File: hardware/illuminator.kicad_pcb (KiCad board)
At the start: 4 copper layers, 85 x 100 mm, 63 parts, among them J101 HRO_TYPE_C_31_M_12, J102 PROG, J103 LCLV, Q201 DMP3028, Q202 MMBT3904, SW101 RESET, SW102 DFU, U101 SRV05-4, U102 STM32G431CBUx, U103 WAS3157B-6/TR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

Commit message: heatsinking
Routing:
- net GND: vias 46 -> 48
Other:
- board text added: "mateijordache.info"
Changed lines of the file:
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@@
 		(fp_arc
 			(start 10.656836 20.999983)
-			(mid 9.891462 20.847753)
+			(mid 9.891468 20.847747)
 			(end 9.242623 20.414196)
 			(stroke
@@
 		(fp_arc
 			(start 30.160875 53.5)
-			(mid 28.989302 56.328429)
+			(mid 28.989302 56.328425)
 			(end 26.160875 57.5)
 			(stroke
@@
 		(tags "tag connect programming header pogo pins")
 		(property "Reference" "J102"
-			(at 0 -2.7 270)
+			(at 0 -2.7 -90)
 			(layer "B.SilkS")
 			(hide yes)
@@
 		)
 		(property "Value" "PROG"
-			(at 0 2.300001 270)
+			(at 0 2.300001 -90)
 			(layer "B.Fab")
 			(effects
@@
 		)
 		(fp_text user "KEEPOUT"
-			(at 0 0 270)
+			(at 0 0 -90)
 			(layer "Cmts.User")
 			(effects
@@
 		)
 		(fp_text user "${REFERENCE}"
-			(at 0 0 270)
+			(at 0 0 -90)
 			(layer "B.Fab")
 			(effects
@@
 		(net 7)
 	)
+	(gr_arc
+		(start 136.5985 121.498499)
+		(mid 150.421081 57.916367)
+		(end 164.91972 121.347753)
+		(stroke
+			(width 12)
+			(type default)
+		)
+		(layer "B.Mask")
+	)
+	(gr_text "mateijordache.info"
+		(at 161.4235 115.0735 0)
+		(layer "B.Mask")
+		(effects
+			(font
+				(size 1.5 1.5)
+				(thickness 0.3)
+				(bold yes)
+			)
+			(justify left bottom mirror)
+		)
+	)
 	(segment
 		(start 150.7485 145.5235)
@@
 	)
 	(segment
-		(start 146.0485 146.4985)
-		(end 150.7485 146.4985)
-		(width 0.25)
-		(layer "B.Cu")
-		(net 1)
-	)
-	(segment
 		(start 137.6485 137.8985)
 		(end 144.5885 137.8985)
@@
 	)
 	(segment
-		(start 145.3235 145.7735)
-		(end 146.0485 146.4985)
-		(width 0.25)
-		(layer "B.Cu")
-		(net 1)
-	)
-	(segment
 		(start 151.0235 145.5235)
 		(end 151.0485 145.4985)
@@
 	)
 	(segment
-		(start 136.1585 134.1585)
-		(end 135.4985 134.8185)
+		(start 145.2985 138.6085)
+		(end 145.3235 138.6335)
+		(width 0.25)
+		(layer "B.Cu")
+		(net 1)
+	)
+	(segment
+		(start 146.7985 146.4985)
+		(end 150.7485 146.4985)
 		(width 0.25)
 		(layer "B.Cu")
@@
 	(segment
 		(start 145.3235 138.6335)
-		(end 145.3235 145.7735)
+		(end 145.3235 145.0235)
 		(width 0.25)
 		(layer "B.Cu")
@@
 	)
 	(segment
-		(start 145.2985 138.6085)
-		(end 145.3235 138.6335)
+		(start 136.1585 134.1585)
+		(end 135.4985 134.8185)
+		(width 0.25)
+		(layer "B.Cu")
+		(net 1)
+	)
+	(segment
+		(start 145.3235 145.0235)
+		(end 146.7985 146.4985)
 		(width 0.25)
 		(layer "B.Cu")
@@
 	)
 	(via
+		(at 155.4985 137.1735)
+		(size 0.8)
+		(drill 0.4)
+		(layers "F.Cu" "B.Cu")
+		(free yes)
+		(net 2)
+	)
+	(via
 		(at 149.2985 141.0485)
 		(size 0.8)
@@
 	)
 	(via
+		(at 155.4985 138.6985)
+		(size 0.8)
+		(drill 0.4)
+		(layers "F.Cu" "B.Cu")
+		(free yes)
+		(net 2)
+	)
+	(via
 		(at 177.5735 108.6235)
 		(size 0.8)
@@
 	)
 	(segment
-		(start 159.7985 131.3985)
-		(end 159.7985 136.886)
+		(start 154.7485 117.8635)
+		(end 154.7485 118.9235)
 		(width 0.25)
 		(layer "B.Cu")
@@
 	)
 	(segment
-		(start 154.7485 119.0485)
-		(end 157.2235 121.5235)
+		(start 154.7485 118.9235)
+		(end 156.8485 121.0235)
 		(width 0.25)
 		(layer "B.Cu")
@@
 	)
 	(segment
-		(start 154.7485 117.8635)
-		(end 154.7485 119.0485)
+		(start 156.8485 121.0235)
+		(end 156.8485 128.711)
 		(width 0.25)
 		(layer "B.Cu")
@@
 	)
 	(segment
-		(start 157.2235 128.8235)
-		(end 159.7985 131.3985)
+		(start 159.5485 131.411)
+		(end 159.5485 136.636)
 		(width 0.25)
 		(layer "B.Cu")
@@
 	)
 	(segment
-		(start 159.7985 136.886)
+		(start 159.5485 136.636)
 		(end 161.4985 138.586)
 		(width 0.25)
@@
 	)
 	(segment
-		(start 157.2235 121.5235)
-		(end 157.2235 128.8235)
+		(start 156.8485 128.711)
+		(end 159.5485 131.411)
 		(width 0.25)
 		(layer "B.Cu")
@@
 	)
 	(segment
+		(start 144.7985 129.3485)
+		(end 139.9885 134.1585)
+		(width 0.1)
+		(layer "B.Cu")
+		(net 32)
+	)
+	(segment
 		(start 153.0235 129.4235)
 		(end 152.9485 129.3485)
@@
 	)
 	(segment
-		(start 152.9485 129.3485)
-		(end 142.2385 129.3485)
+		(start 139.9885 134.1585)
+		(end 137.4285 134.1585)
 		(width 0.1)
 		(layer "B.Cu")
@@
 	)
 	(segment
-		(start 142.2385 129.3485)
-		(end 137.4285 134.1585)
+		(start 152.9485 129.3485)
+		(end 144.7985 129.3485)
 		(width 0.1)
 		(layer "B.Cu")
@@
 	)
 	(segment
-		(start 152.4485 128.8485)
-		(end 141.4685 128.8485)
+		(start 144.5235 128.8485)
+		(end 140.4835 132.8885)
 		(width 0.1)
 		(layer "B.Cu")
@@
 	)
 	(segment
-		(start 141.4685 128.8485)
+		(start 140.4835 132.8885)
 		(end 137.4285 132.8885)
 		(width 0.1)
@@
 	)
 	(segment
+		(start 152.4485 128.8485)
+		(end 144.5235 128.8485)
+		(width 0.1)
+		(layer "B.Cu")
+		(net 33)
+	)
+	(segment
 		(start 145.3485 135.6985)
 		(end 145.0235 136.0235)
@@
 	)
 	(segment
-		(start 141.3235 128.1235)
-		(end 137.8285 131.6185)
+		(start 151.9485 128.1235)
+		(end 144.4235 128.1235)
 		(width 0.1)
 		(layer "B.Cu")
@@
 	)
 	(segment
-		(start 151.9485 128.1235)
-		(end 141.3235 128.1235)
+		(start 140.9285 131.6185)
+		(end 137.4285 131.6185)
 		(width 0.1)
 		(layer "B.Cu")
@@
 	)
 	(segment
-		(start 137.8285 131.6185)
-		(end 137.4285 131.6185)
+		(start 144.4235 128.1235)
+		(end 140.9285 131.6185)
 		(width 0.1)
 		(layer "B.Cu")
@@
 	)
 	(segment
-		(start 166.8735 144.1985)
-		(end 166.8735 141.8485)
+		(start 168.7235 139.9985)
+		(end 172.2765 139.9985)
 		(width 0.1)
 		(layer "B.Cu")
@@
 	)
 	(segment
-		(start 146.0235 137.8735)
-		(end 146.5235 138.3735)
-		(width 0.1)
-		(layer "B.Cu")
-		(net 42)
-	)
-	(segment
-		(start 166.8735 141.8485)
-		(end 168.7235 139.9985)
+		(start 150.4735 144.5985)
+		(end 166.4735 144.5985)
 		(width 0.1)
 		(layer "B.Cu")
@@
 	)
 	(segment
-		(start 146.9485 145.7235)
-		(end 148.817954 145.7235)
+		(start 146.0235 137.8735)
+		(end 146.0235 144.8235)
 		(width 0.1)
 		(layer "B.Cu")
@@
 	)
 	(segment
-		(start 168.7235 139.9985)
-		(end 172.2765 139.9985)
+		(start 166.8735 141.8485)
+		(end 168.7235 139.9985)
 		(width 0.1)
 		(layer "B.Cu")
@@
 	)
 	(segment
-		(start 148.817954 145.7235)
-		(end 149.942954 144.5985)
+		(start 166.4735 144.5985)
+		(end 166.8735 144.1985)
 		(width 0.1)
 		(layer "B.Cu")
@@
 	)
 	(segment
-		(start 146.5235 145.2985)
-		(end 146.9485 145.7235)
+		(start 146.0235 144.8235)
+		(end 147.0985 145.8985)
 		(width 0.1)
 		(layer "B.Cu")
@@
 	)
 	(segment
-		(start 146.5235 138.3735)
-		(end 146.5235 145.2985)
+		(start 147.0985 145.8985)
+		(end 149.1735 145.8985)
 		(width 0.1)
 		(layer "B.Cu")
@@
 	)
 	(segment
-		(start 149.942954 144.5985)
-		(end 166.4735 144.5985)
+		(start 149.1735 145.8985)
+		(end 150.4735 144.5985)
 		(width 0.1)
 		(layer "B.Cu")
@@
 	)
 	(segment
-		(start 166.4735 144.5985)
-		(end 166.8735 144.1985)
+		(start 166.8735 144.1985)
+		(end 166.8735 141.8485)
 		(width 0.1)
 		(layer "B.Cu")

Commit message: fix bom
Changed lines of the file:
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@@
 			(viasonmask no)
 			(mode 1)
-			(useauxorigin no)
+			(useauxorigin yes)
 			(hpglpennumber 1)
 			(hpglpenspeed 20)
@@
 			(outputformat 1)
 			(mirror no)
-			(drillshape 1)
+			(drillshape 0)
 			(scaleselection 1)
-			(outputdirectory "")
+			(outputdirectory "/Users/mateijordache/Desktop/gerbs/")
 		)
 	)
@@
 		(fp_arc
 			(start 10.656836 20.999983)
-			(mid 9.891468 20.847747)
+			(mid 9.891462 20.847753)
 			(end 9.242623 20.414196)
 			(stroke
@@
 		(fp_arc
 			(start 30.160875 53.5)
-			(mid 28.989302 56.328425)
+			(mid 28.989302 56.328429)
 			(end 26.160875 57.5)
 			(stroke

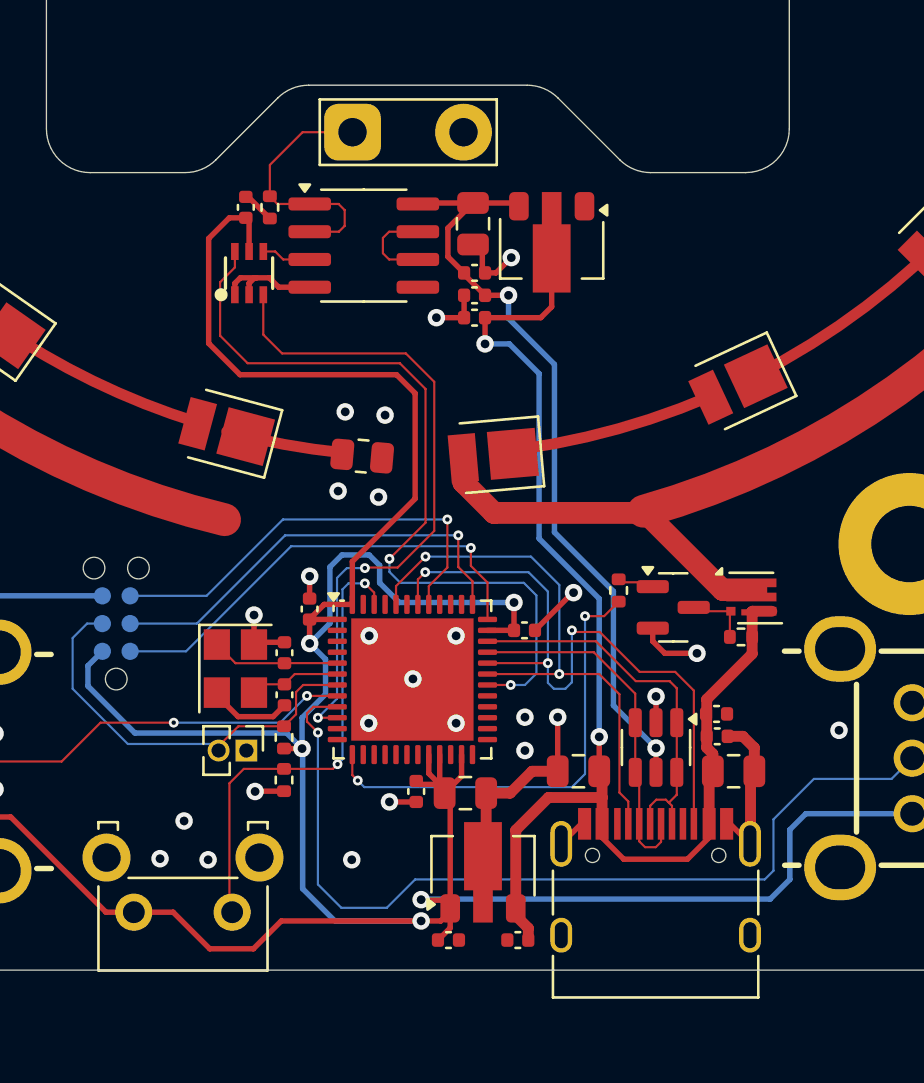
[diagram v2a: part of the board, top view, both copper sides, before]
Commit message: add gain resistors
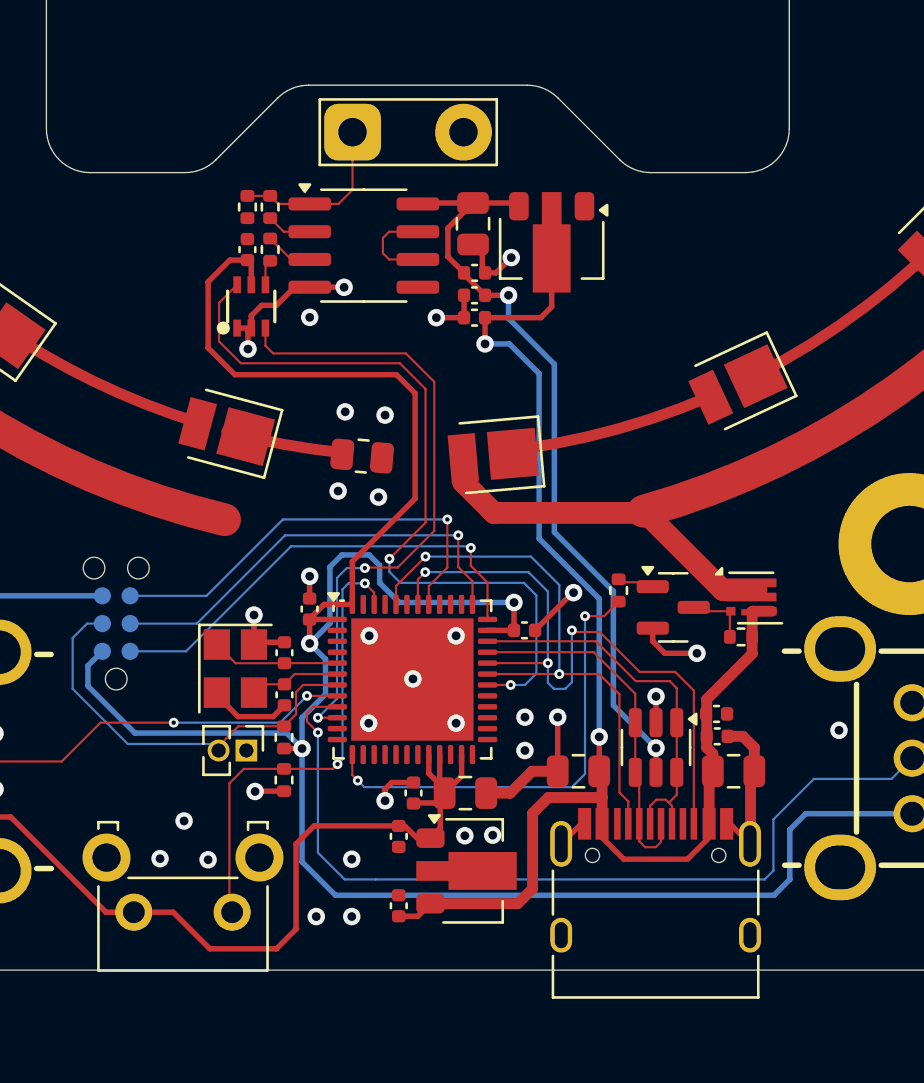
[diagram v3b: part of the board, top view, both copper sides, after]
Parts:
- added R104: 0R, Resistor_SMD:R_0402_1005Metric, F.Cu at (143.8, 115.8)
- added R105: 0R, Resistor_SMD:R_0402_1005Metric, F.Cu at (143.8, 113.8)
- R203, R204, R205, R206, R207, R208: value 50R -> 75R
- moved C112 5.67 mm to (149.7, 145.8), turned to 90 degrees
- moved C113 5.26 mm to (149.7, 142.6), turned to -90 degrees
- moved C105 1.94 mm to (142.8, 115.8)
- moved U103 1.53 mm to (143.0, 118.4)
- moved R103 1.03 mm to (142.8, 113.8)
- moved U106 0.51 mm to (153.1, 144.2), turned to 0 degrees
- moved C103 0.14 mm to (150.4, 140.6), turned to 90 degrees
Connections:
- U104 pad 2: Net-(J103-Pin_1) -> Net-(U104A--)
- U104 pad 3: Net-(U103-A) -> Net-(U104A-+)
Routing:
- net +3V3: track 151.4 -> 144.2 mm, vias 5 -> 3
- net GND: track 58.0 -> 53.8 mm, vias 48 -> 55
- net Net-(J103-Pin_1): track 12.0 -> 7.87 mm
- net VBUS: track 62.3 -> 66.1 mm
- net Net-(U104A-+): track 0.00 -> 2.21 mm
- net Net-(U104A--): track 0.00 -> 2.07 mm
- net /ADC1_IN2: track 41.4 -> 39.5 mm
- net /OPAMP1_VOUT: track 30.4 -> 29.0 mm
- net /TIM1_CH1: track 36.8 -> 35.5 mm
- net Net-(U103-A): track 2.28 -> 1.19 mm

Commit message: fix drc
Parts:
- added R106: 10k, Resistor_SMD:R_0402_1005Metric, F.Cu at (155.1, 136.3)
- moved C104 1.06 mm to (155.1, 132.2), turned to 90 degrees
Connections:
- U103 pad 1: GND -> /OPAMP1_VOUT
- U103 pad 3: /OPAMP1_VOUT -> GND
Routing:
- net +3V3: track 144.2 -> 148.2 mm
- net GND: track 53.8 -> 52.3 mm
- net /OPAMP1_VOUT: track 29.0 -> 30.2 mm
- net /DFU: track 21.6 -> 22.2 mm
